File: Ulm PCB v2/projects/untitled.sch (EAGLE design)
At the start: 26 parts, among them U1 FT232RLSSOP, U2 MCP73831, U3 SPX3819-3.3, X2 USB-SMD-NS

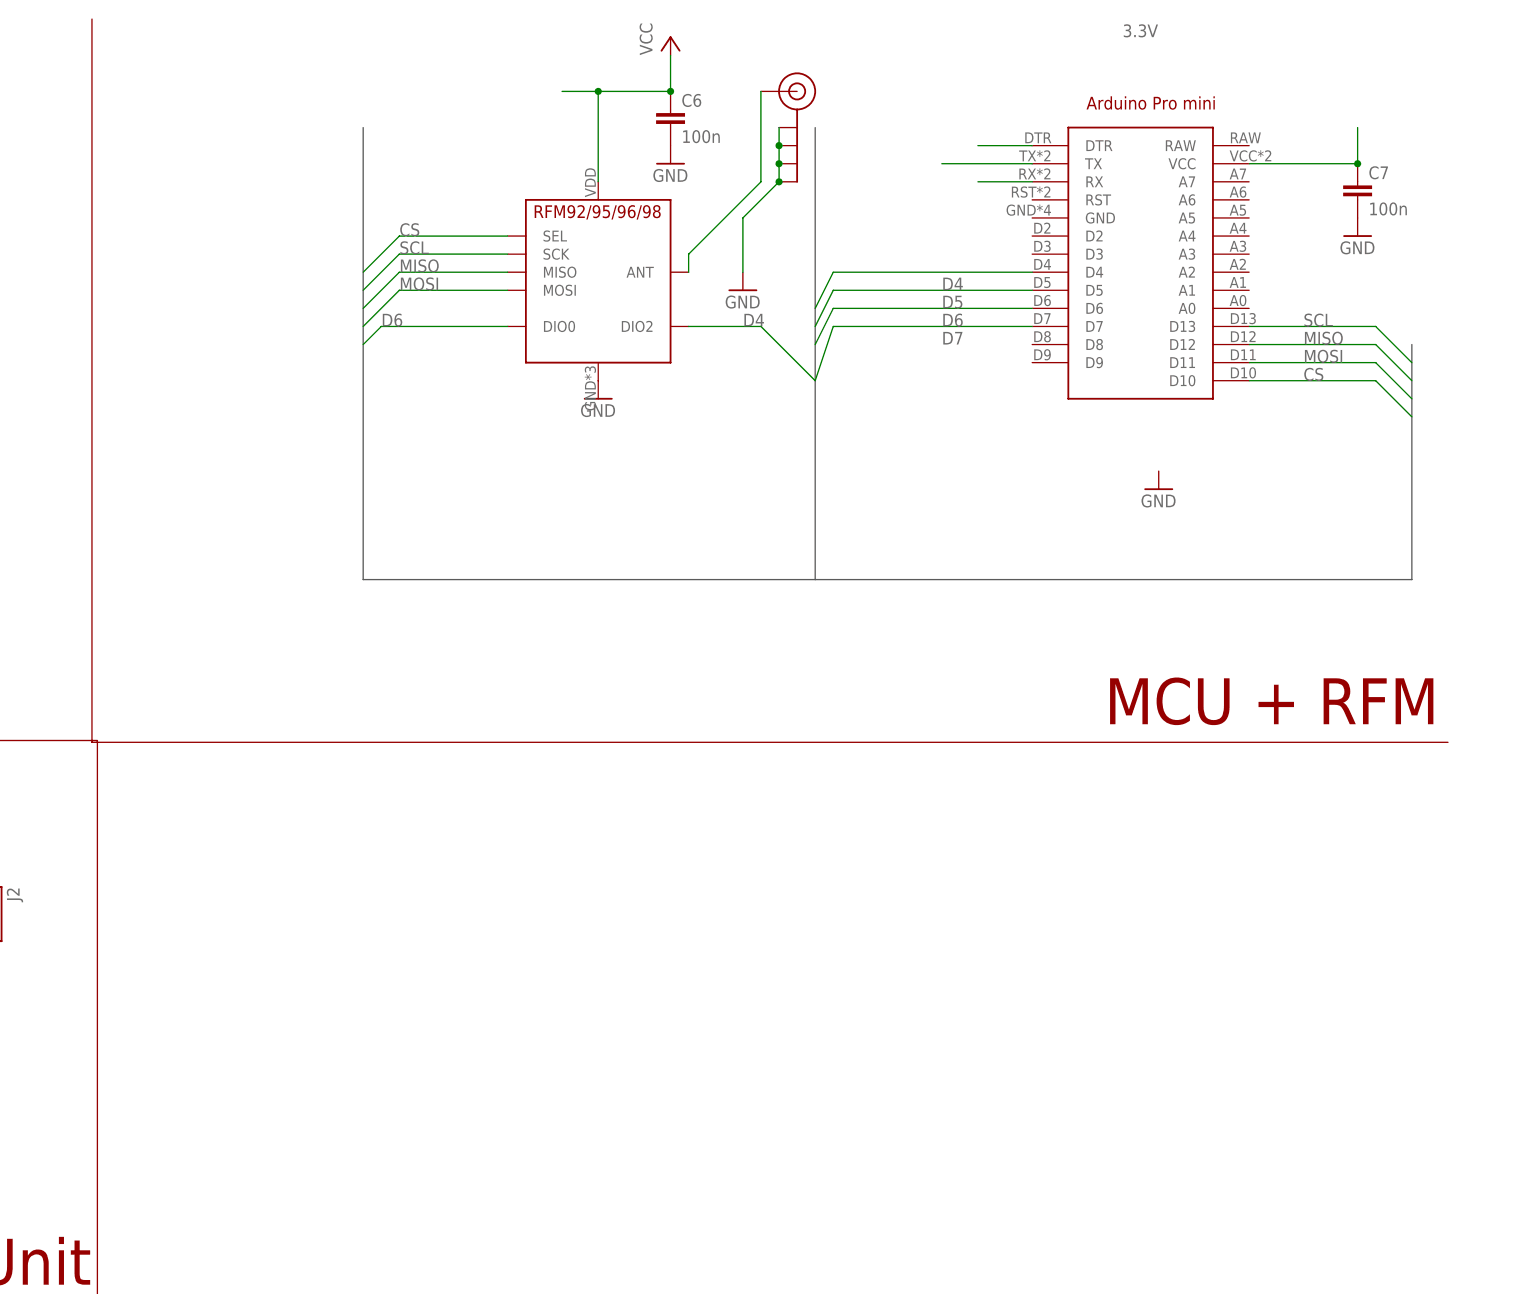
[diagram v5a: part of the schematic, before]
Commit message: Fixed Bug regarding Pinout of RFM95W
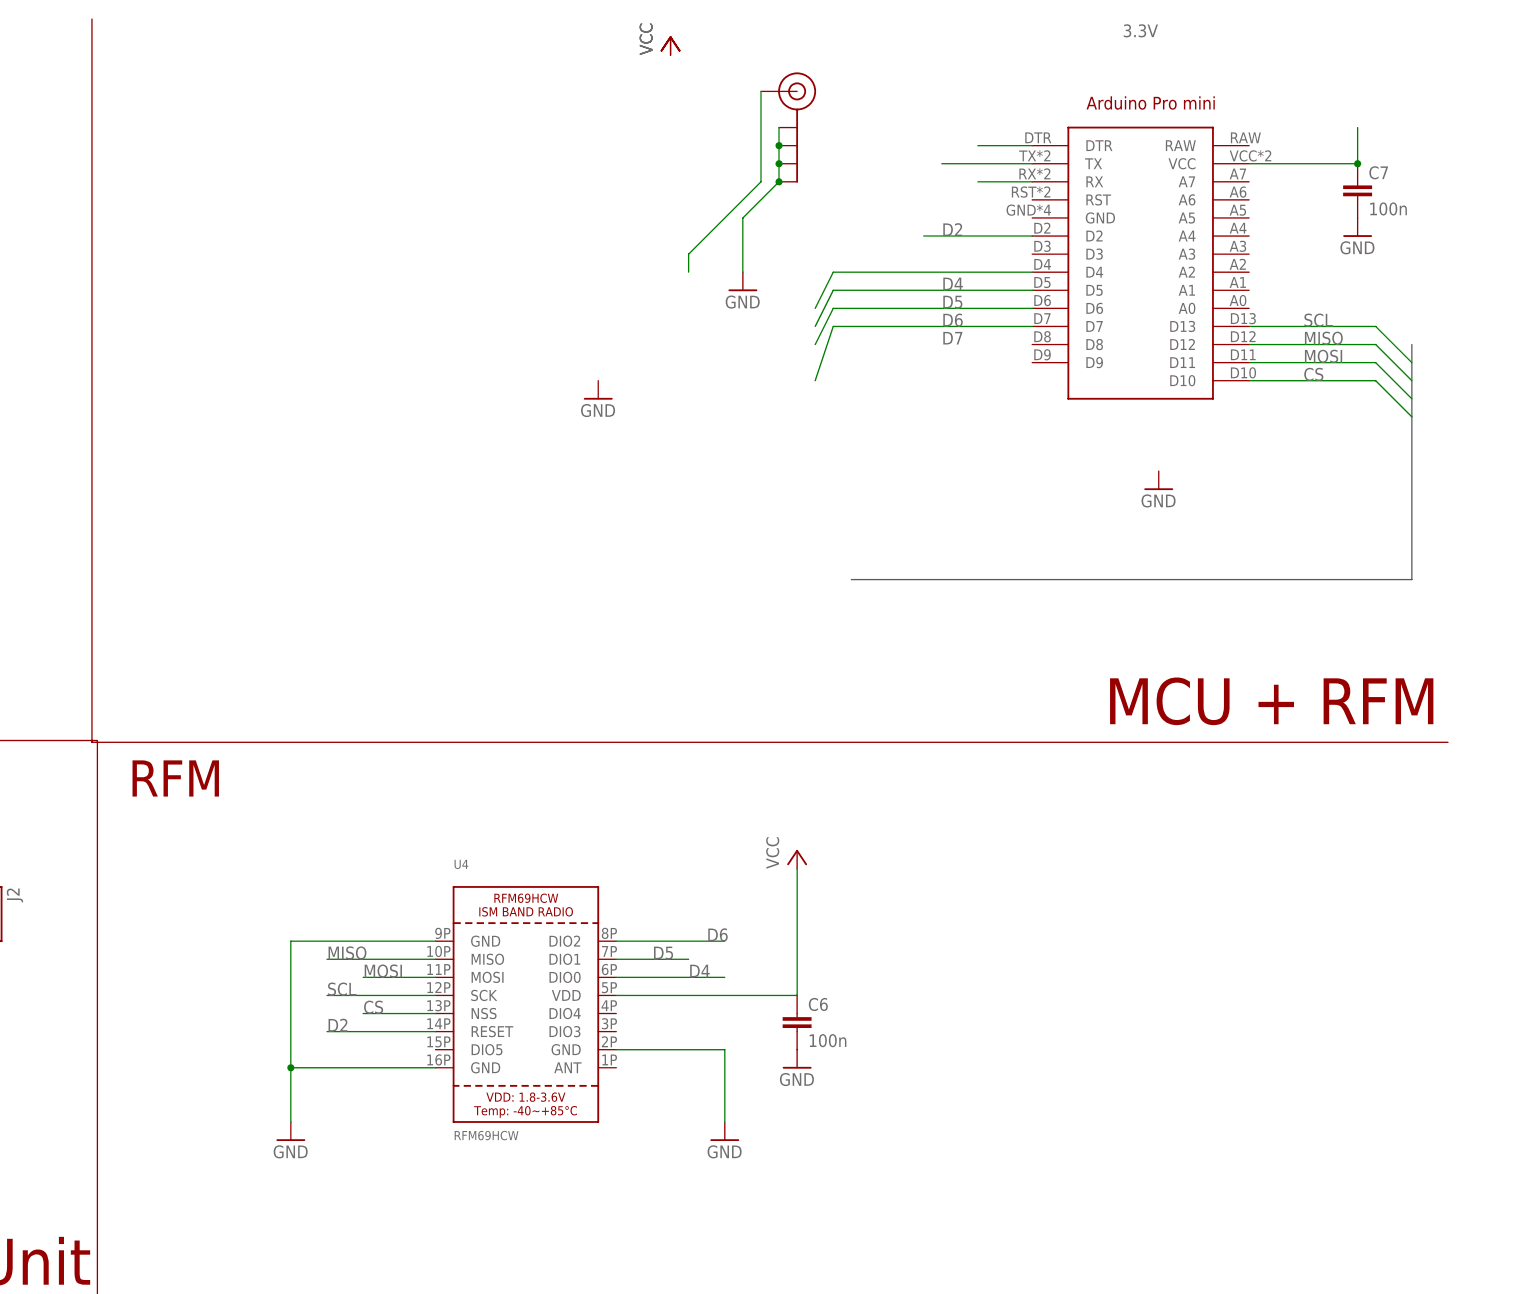
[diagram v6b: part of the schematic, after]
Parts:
- removed U$6: RFM95, _c2h:RFM95
- added U4: RFM69HCW, microbuilder:RFM69HCW_SMT
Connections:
- new net D2: U$1.D2, U4.RESET
- new net N$16: U4.GND@1
- new net VCC: U4.VDD
- net 3.3V: no longer C6.1, U$6.VCC
- net CS: now also U4.NSS; no longer U$6.SEL
- net D4: now also U4.DIO0; no longer U$6.DIO2
- net D5: now also U4.DIO1
- net D6: now also U4.DIO2; no longer U$6.DIO0
- net GND: now also U4.GND@2, U4.GND@3; no longer U$6.GND
- net MISO: now also U4.MISO; no longer U$6.MISO
- net MOSI: now also U4.MOSI; no longer U$6.MOSI
- net N$4: no longer U$6.ANT
- net SCL: now also U4.SCK; no longer U$6.SCK
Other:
- note added: "RFM"
- moved on the sheet: C6
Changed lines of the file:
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@@
 <part name="C6" library="rcl" library_urn="urn:adsk.eagle:library:334" deviceset="C-EU" device="C0805" value="100n"/>
 <part name="C7" library="rcl" deviceset="C-EU" device="C0805" value="100n"/>
-<part name="U$6" library="_c2h" deviceset="RFM95" device=""/>
 <part name="GND15" library="supply1" deviceset="GND" device=""/>
 <part name="GND13" library="supply1" deviceset="GND" device=""/>
@@
 <part name="+3V1" library="supply1" deviceset="+3V3" device="" value="3.3V"/>
 <part name="J$2" library="_c2h" deviceset="ANTENNA" device="TINY"/>
+<part name="U4" library="microbuilder" deviceset="RFM69HCW" device="_SMT" value="RFM69HCW"/>
+<part name="GND1" library="supply1" deviceset="GND" device=""/>
+<part name="GND10" library="supply1" deviceset="GND" device=""/>
+<part name="P+2" library="supply1" deviceset="VCC" device=""/>
+<part name="P+4" library="supply1" deviceset="VCC" device=""/>
 </parts>
 <sheets>
@@
 <wire x1="22.86" y1="335.28" x2="22.86" y2="436.88" width="0.1524" layer="94"/>
 <text x="165.1" y="337.82" size="6.4516" layer="94">MCU + RFM</text>
+<text x="27.94" y="327.66" size="5.08" layer="94">RFM</text>
 </plain>
 <instances>
@@
 <instance part="GND9" gate="1" x="-2.54" y="284.48"/>
 <instance part="P+3" gate="VCC" x="104.14" y="434.34"/>
-<instance part="C6" gate="G$1" x="104.14" y="424.18"/>
+<instance part="C6" gate="G$1" x="121.92" y="297.18"/>
 <instance part="C7" gate="G$1" x="200.66" y="414.02"/>
-<instance part="U$6" gate="G$1" x="93.98" y="401.32"/>
-<instance part="GND15" gate="1" x="104.14" y="416.56"/>
+<instance part="GND15" gate="1" x="121.92" y="289.56"/>
 <instance part="GND13" gate="1" x="93.98" y="383.54"/>
 <instance part="GND16" gate="1" x="114.3" y="398.78"/>
@@
 <instance part="+3V1" gate="G$1" x="-139.7" y="325.12" rot="MR0"/>
 <instance part="J$2" gate="1" x="121.92" y="426.72"/>
+<instance part="U4" gate="G$1" x="83.82" y="299.72"/>
+<instance part="GND1" gate="1" x="50.8" y="279.4"/>
+<instance part="GND10" gate="1" x="111.76" y="279.4"/>
+<instance part="P+2" gate="VCC" x="104.14" y="434.34"/>
+<instance part="P+4" gate="VCC" x="121.92" y="320.04"/>
 </instances>
 <busses>
@@
 <segment>
 <wire x1="208.28" y1="391.16" x2="208.28" y2="358.14" width="0.762" layer="92"/>
-<wire x1="208.28" y1="358.14" x2="124.46" y2="358.14" width="0.762" layer="92"/>
-<wire x1="124.46" y1="358.14" x2="124.46" y2="421.64" width="0.762" layer="92"/>
-<wire x1="124.46" y1="358.14" x2="60.96" y2="358.14" width="0.762" layer="92"/>
-<wire x1="60.96" y1="358.14" x2="60.96" y2="421.64" width="0.762" layer="92"/>
+<wire x1="208.28" y1="358.14" x2="129.54" y2="358.14" width="0.762" layer="92"/>
 </segment>
 </bus>
@@
 </segment>
 <segment>
-<pinref part="U$6" gate="G$1" pin="GND"/>
-<pinref part="GND13" gate="1" pin="GND"/>
-</segment>
-<segment>
 <wire x1="114.3" y1="408.94" x2="114.3" y2="401.32" width="0.1524" layer="91"/>
 <pinref part="GND16" gate="1" pin="GND"/>
@@
 <pinref part="U$30" gate="G$1" pin="GND"/>
 </segment>
+<segment>
+<pinref part="U4" gate="G$1" pin="GND@2"/>
+<wire x1="71.12" y1="307.34" x2="50.8" y2="307.34" width="0.1524" layer="91"/>
+<wire x1="50.8" y1="307.34" x2="50.8" y2="289.56" width="0.1524" layer="91"/>
+<pinref part="U4" gate="G$1" pin="GND@3"/>
+<wire x1="50.8" y1="289.56" x2="50.8" y2="281.94" width="0.1524" layer="91"/>
+<wire x1="71.12" y1="289.56" x2="50.8" y2="289.56" width="0.1524" layer="91"/>
+<junction x="50.8" y="289.56"/>
+<pinref part="GND1" gate="1" pin="GND"/>
+</segment>
 </net>
 <net name="USB_D-" class="0">
@@
 </segment>
 <segment>
-<wire x1="88.9" y1="426.72" x2="93.98" y2="426.72" width="0.1524" layer="91"/>
 <pinref part="P+3" gate="VCC" pin="VCC"/>
-<pinref part="C6" gate="G$1" pin="1"/>
-<wire x1="93.98" y1="426.72" x2="104.14" y2="426.72" width="0.1524" layer="91"/>
-<wire x1="104.14" y1="426.72" x2="104.14" y2="431.8" width="0.1524" layer="91"/>
-<junction x="104.14" y="426.72"/>
-<pinref part="U$6" gate="G$1" pin="VCC"/>
-<wire x1="93.98" y1="414.02" x2="93.98" y2="426.72" width="0.1524" layer="91"/>
-<junction x="93.98" y="426.72"/>
+<pinref part="P+2" gate="VCC" pin="VCC"/>
 </segment>
 <segment>
@@
 </segment>
 <segment>
-<pinref part="U$6" gate="G$1" pin="SCK"/>
-<wire x1="81.28" y1="403.86" x2="66.04" y2="403.86" width="0.1524" layer="91"/>
-<wire x1="66.04" y1="403.86" x2="60.96" y2="398.78" width="0.1524" layer="91"/>
-<label x="66.04" y="403.86" size="1.778" layer="95"/>
+<pinref part="U4" gate="G$1" pin="SCK"/>
+<wire x1="71.12" y1="299.72" x2="55.88" y2="299.72" width="0.1524" layer="91"/>
+<label x="55.88" y="299.72" size="1.778" layer="95"/>
 </segment>
 </net>
@@
 </segment>
 <segment>
-<pinref part="U$6" gate="G$1" pin="MISO"/>
-<wire x1="81.28" y1="401.32" x2="66.04" y2="401.32" width="0.1524" layer="91"/>
-<wire x1="66.04" y1="401.32" x2="60.96" y2="396.24" width="0.1524" layer="91"/>
-<label x="66.04" y="401.32" size="1.778" layer="95"/>
+<pinref part="U4" gate="G$1" pin="MISO"/>
+<wire x1="71.12" y1="304.8" x2="55.88" y2="304.8" width="0.1524" layer="91"/>
+<label x="55.88" y="304.8" size="1.778" layer="95"/>
 </segment>
 </net>
@@
 </segment>
 <segment>
-<pinref part="U$6" gate="G$1" pin="MOSI"/>
-<wire x1="81.28" y1="398.78" x2="66.04" y2="398.78" width="0.1524" layer="91"/>
-<wire x1="66.04" y1="398.78" x2="60.96" y2="393.7" width="0.1524" layer="91"/>
-<label x="66.04" y="398.78" size="1.778" layer="95"/>
+<pinref part="U4" gate="G$1" pin="MOSI"/>
+<wire x1="71.12" y1="302.26" x2="60.96" y2="302.26" width="0.1524" layer="91"/>
+<label x="60.96" y="302.26" size="1.778" layer="95"/>
 </segment>
 </net>
@@
 </segment>
 <segment>
-<pinref part="U$6" gate="G$1" pin="SEL"/>
-<wire x1="81.28" y1="406.4" x2="66.04" y2="406.4" width="0.1524" layer="91"/>
-<wire x1="66.04" y1="406.4" x2="60.96" y2="401.32" width="0.1524" layer="91"/>
-<label x="66.04" y="406.4" size="1.778" layer="95"/>
+<pinref part="U4" gate="G$1" pin="NSS"/>
+<wire x1="71.12" y1="297.18" x2="60.96" y2="297.18" width="0.1524" layer="91"/>
+<label x="60.96" y="297.18" size="1.778" layer="95"/>
 </segment>
 </net>
@@
 <wire x1="127" y1="398.78" x2="124.46" y2="393.7" width="0.1524" layer="91"/>
 </segment>
+<segment>
+<pinref part="U4" gate="G$1" pin="DIO1"/>
+<wire x1="96.52" y1="304.8" x2="106.68" y2="304.8" width="0.1524" layer="91"/>
+<label x="101.6" y="304.8" size="1.778" layer="95"/>
+</segment>
 </net>
 <net name="D4" class="0">
@@
 </segment>
 <segment>
-<pinref part="U$6" gate="G$1" pin="DIO2"/>
-<wire x1="106.68" y1="393.7" x2="116.84" y2="393.7" width="0.1524" layer="91"/>
-<wire x1="116.84" y1="393.7" x2="124.46" y2="386.08" width="0.1524" layer="91"/>
-<label x="114.3" y="393.7" size="1.778" layer="95"/>
+<pinref part="U4" gate="G$1" pin="DIO0"/>
+<wire x1="96.52" y1="302.26" x2="111.76" y2="302.26" width="0.1524" layer="91"/>
+<label x="106.68" y="302.26" size="1.778" layer="95"/>
 </segment>
 </net>
@@
 </segment>
 <segment>
-<pinref part="U$6" gate="G$1" pin="DIO0"/>
-<wire x1="81.28" y1="393.7" x2="63.5" y2="393.7" width="0.1524" layer="91"/>
-<wire x1="63.5" y1="393.7" x2="60.96" y2="391.16" width="0.1524" layer="91"/>
-<label x="63.5" y="393.7" size="1.778" layer="95"/>
+<pinref part="U4" gate="G$1" pin="DIO2"/>
+<wire x1="96.52" y1="307.34" x2="111.76" y2="307.34" width="0.1524" layer="91"/>
+<label x="109.22" y="307.34" size="1.778" layer="95"/>
 </segment>
 </net>
 <net name="N$4" class="0">
 <segment>
-<pinref part="U$6" gate="G$1" pin="ANT"/>
 <wire x1="106.68" y1="401.32" x2="106.68" y2="403.86" width="0.1524" layer="91"/>
 <wire x1="106.68" y1="403.86" x2="116.84" y2="414.02" width="0.1524" layer="91"/>
@@
 </segment>
 </net>
+<net name="N$16" class="0">
+<segment>
+<pinref part="U4" gate="G$1" pin="GND@1"/>
+<wire x1="96.52" y1="292.1" x2="111.76" y2="292.1" width="0.1524" layer="91"/>
+<wire x1="111.76" y1="292.1" x2="111.76" y2="281.94" width="0.1524" layer="91"/>
+</segment>
+</net>
+<net name="VCC" class="0">
+<segment>
+<pinref part="U4" gate="G$1" pin="VDD"/>
+<wire x1="96.52" y1="299.72" x2="121.92" y2="299.72" width="0.1524" layer="91"/>
+<wire x1="121.92" y1="299.72" x2="121.92" y2="317.5" width="0.1524" layer="91"/>
+<pinref part="P+4" gate="VCC" pin="VCC"/>
+</segment>
+</net>
+<net name="D2" class="0">
+<segment>
+<pinref part="U$1" gate="G$1" pin="D2"/>
+<wire x1="154.94" y1="406.4" x2="139.7" y2="406.4" width="0.1524" layer="91"/>
+<label x="142.24" y="406.4" size="1.778" layer="95"/>
+</segment>
+<segment>
+<pinref part="U4" gate="G$1" pin="RESET"/>
+<wire x1="71.12" y1="294.64" x2="55.88" y2="294.64" width="0.1524" layer="91"/>
+<label x="55.88" y="294.64" size="1.778" layer="95"/>
+</segment>
+</net>
 </nets>
 </sheet>
@@
 </drawing>
 <compatibility>
+<note version="6.3" minversion="6.2.2" severity="warning">
+Since Version 6.2.2 text objects can contain more than one line,
+which will not be processed correctly with this version.
+</note>
 <note version="8.2" severity="warning">
 Since Version 8.2, EAGLE supports online libraries. The ids

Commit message: corrected DRC-Errors. ToDo: Right USB Slot, Diode vs. Jumper
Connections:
- removed net N$4: J$2.SIGNAL
- new net ANT: J$2.SIGNAL, U4.ANT
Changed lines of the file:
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@@
 <instance part="GND15" gate="1" x="121.92" y="289.56"/>
 <instance part="GND13" gate="1" x="93.98" y="383.54"/>
-<instance part="GND16" gate="1" x="114.3" y="398.78"/>
+<instance part="GND16" gate="1" x="157.48" y="281.94"/>
 <instance part="C8" gate="G$1" x="-154.94" y="403.86"/>
 <instance part="C9" gate="G$1" x="-109.22" y="403.86"/>
@@
 <instance part="R4" gate="G$1" x="-147.32" y="411.48" rot="R270"/>
 <instance part="+3V1" gate="G$1" x="-139.7" y="325.12" rot="MR0"/>
-<instance part="J$2" gate="1" x="121.92" y="426.72"/>
+<instance part="J$2" gate="1" x="165.1" y="309.88"/>
 <instance part="U4" gate="G$1" x="83.82" y="299.72"/>
 <instance part="GND1" gate="1" x="50.8" y="279.4"/>
@@
 </segment>
 <segment>
-<wire x1="114.3" y1="408.94" x2="114.3" y2="401.32" width="0.1524" layer="91"/>
+<wire x1="157.48" y1="292.1" x2="157.48" y2="284.48" width="0.1524" layer="91"/>
 <pinref part="GND16" gate="1" pin="GND"/>
-<wire x1="119.38" y1="421.64" x2="119.38" y2="419.1" width="0.1524" layer="91"/>
-<wire x1="119.38" y1="419.1" x2="119.38" y2="416.56" width="0.1524" layer="91"/>
-<wire x1="119.38" y1="416.56" x2="119.38" y2="414.02" width="0.1524" layer="91"/>
-<wire x1="114.3" y1="408.94" x2="119.38" y2="414.02" width="0.1524" layer="91"/>
+<wire x1="162.56" y1="304.8" x2="162.56" y2="302.26" width="0.1524" layer="91"/>
+<wire x1="162.56" y1="302.26" x2="162.56" y2="299.72" width="0.1524" layer="91"/>
+<wire x1="162.56" y1="299.72" x2="162.56" y2="297.18" width="0.1524" layer="91"/>
+<wire x1="157.48" y1="292.1" x2="162.56" y2="297.18" width="0.1524" layer="91"/>
 <pinref part="J$2" gate="1" pin="GND@0"/>
 <pinref part="J$2" gate="1" pin="GND@1"/>
-<junction x="119.38" y="419.1"/>
+<junction x="162.56" y="302.26"/>
 <pinref part="J$2" gate="1" pin="GND@2"/>
-<junction x="119.38" y="416.56"/>
+<junction x="162.56" y="299.72"/>
 <pinref part="J$2" gate="1" pin="GND@3"/>
-<junction x="119.38" y="414.02"/>
+<junction x="162.56" y="297.18"/>
 </segment>
 <segment>
@@
 </segment>
 </net>
-<net name="N$4" class="0">
-<segment>
-<wire x1="106.68" y1="401.32" x2="106.68" y2="403.86" width="0.1524" layer="91"/>
-<wire x1="106.68" y1="403.86" x2="116.84" y2="414.02" width="0.1524" layer="91"/>
-<wire x1="116.84" y1="426.72" x2="116.84" y2="414.02" width="0.1524" layer="91"/>
-<pinref part="J$2" gate="1" pin="SIGNAL"/>
-</segment>
-</net>
 <net name="VBAT" class="0">
 <segment>
@@
 </segment>
 </net>
+<net name="ANT" class="0">
+<segment>
+<pinref part="U4" gate="G$1" pin="ANT"/>
+<wire x1="96.52" y1="289.56" x2="104.14" y2="289.56" width="0.1524" layer="91"/>
+<label x="99.06" y="289.56" size="1.778" layer="95"/>
+</segment>
+<segment>
+<pinref part="J$2" gate="1" pin="SIGNAL"/>
+<wire x1="160.02" y1="309.88" x2="139.7" y2="309.88" width="0.1524" layer="91"/>
+<label x="139.7" y="309.88" size="1.778" layer="95"/>
+</segment>
+</net>

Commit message: Final Final
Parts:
- added D3: MBR120, microbuilder:DIODE-SCHOTTKYSOD-123
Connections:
- removed net 5V: C2.1, C5.+, C8.1, D2.C, R4.1, U1.VCC, U2.VIN, U3.IN, X2.VBUS
- new net V5: C8.1, D2.C, D3.C, R4.1, U2.VIN, U3.IN
- new net VBUS: C2.1, C5.+, D3.A, U1.VCC, X2.VBUS
